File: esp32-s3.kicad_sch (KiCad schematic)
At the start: 21 parts, among them J3 Conn_01x07, Q1 2N7002, Q3 S8050, Q4 S8050, SW1 RESET, SW2 BOOT, U3 ESP32-S3-WROOM-1

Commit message: Pre-fab QA review fixes: switch input levels, power path, sensor spec, ESD
- R1-R8 switch series resistors 10k -> 1k: with only the ESP32 internal
  ~45k pull-up, 10k divided a closed switch to 0.6V vs the S3's 0.825V
  VIL limit — marginal. 1k gives ~0.1-0.23V worst case.
- U11 ACS723 -> ACS725LLCTR-05AB-T (C3684552): ACS723 needs 4.5-5.5V but
  ran at 3.3V (out of spec). ACS725 is 3.3V-native, same SOIC-8, rated
  to +150C. Firmware: sensitivity 264mV/A, formula (x-1.65)/0.264.
- D2 BAT54C (200mA) removed; replaced with D10/D11 SS34 (3A) diode-OR.
  The old diode carried the full ESP32 load permanently; WiFi TX bursts
  reach 350-500mA.
- U16 PRTR5V0U2X added on USB D+/D- (ESD protection at J2).
- D1 SS34 -> SS54 (5A, same SMA footprint) for multi-motor headroom.
- C10 bumped to 25V-rated 100uF 1210 (C2840614), same footprint.
- Filled all missing LCSC fields for JLCPCB assembly BOM.
- Docs: J4 pinout corrected to as-built; firmware bring-up checklist and
  RTS/DTR terminal gotcha added; CLAUDE.md placement guide for D10/D11/U16.

PCB placement of D10/D11/U16 + F8 sync still pending.

Co-Authored-By: Claude Fable 5 <noreply@anthropic.com>
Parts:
- C17: LCSC (none) -> C15849
- Q1: LCSC (none) -> C8545
- Q3, Q4: LCSC (none) -> C2146
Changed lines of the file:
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@@
+			)
+		)
+		(property "LCSC" "C8545"
+			(at 207.01 35.56 0)
+			(hide yes)
+			(show_name no)
+			(do_not_autoplace no)
+			(effects
+				(font
+					(size 1.27 1.27)
+				)
 			)
 		)
@@
 			)
 		)
+		(property "LCSC" "C15849"
+			(at 264.16 38.1 0)
+			(hide yes)
+			(show_name no)
+			(do_not_autoplace no)
+			(effects
+				(font
+					(size 1.27 1.27)
+				)
+			)
+		)
 		(pin "1"
 		)
@@
 			)
 		)
+		(property "LCSC" "C2146"
+			(at 262.89 77.47 0)
+			(hide yes)
+			(show_name no)
+			(do_not_autoplace no)
+			(effects
+				(font
+					(size 1.27 1.27)
+				)
+			)
+		)
 		(pin "1"
 		)
@@
 			(at 252.73 38.1 0)
 			(hide yes)
+			(show_name no)
+			(do_not_autoplace no)
+			(effects
+				(font
+					(size 1.27 1.27)
+				)
+			)
+		)
+		(property "LCSC" "C2146"
+			(at 252.73 38.1 0)
+			(hide yes)

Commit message: Rev 1.3 PCB sync + second QA pass: BOM fixes, TVS decoupling, ERC cleanup
PCB (done in KiCad, verified here):
- F8 sync applied: D2 removed; D10/D11 (SS34 SMA) and U16 (PRTR5V0U2X SOT-143)
  placed and routed; R1-R8 -> 1k, D1 -> SS54, C10 -> 25V, U11 -> ACS725 updated
  in place. Footprint-level diff confirms exactly the intended delta, nothing
  else moved. DRC 0 errors / 0 unconnected pads.

Schematic fixes from the second QA pass:
- R1-R8 had NO LCSC part number (value change had landed, part number never
  did) - they would have come back unpopulated, silently killing the switch
  inputs. Set to C14676, matching R14's existing 1K 0603 so it consolidates to
  one BOM line. NOTE: todo.md originally specified C21190 - see the discrepancy
  note there and confirm before ordering.
- TP1-TP7 set in_bom no / in_pos_files no (were 7 junk lines in the JLCPCB BOM).
- Removed 4 orphan dangling wire stubs in switch_inputs.kicad_sch.
- Converted the orphan STBY hierarchical label in motor_drivers.kicad_sch to a
  global label rather than deleting it: its wire actually carried U9 pin 19, so
  deleting dropped U9.19 off the STBY net. Converting keeps the connection and
  clears the ERC hier_label_mismatch.
- Added C40-C43 (100nF 0402, C1525) for U12-U15 VCC decoupling. The switch-input
  TVS devices currently have their nearest +3.3V_ISO bypass 18-23mm away; a
  PRTR5V0U2X shunts ESD into VCC and needs somewhere local to dump it. Still
  need PCB placement - put each within ~2mm of its device's pin 4.

Every schematic edit was validated by diffing the exported netlist before and
after; connectivity is unchanged apart from the four intended new caps.
ERC errors: 10 -> 5 (remaining are 4x missing PWR_FLAG and one J2-GND/U1-(-Vout)
both-power-output pair that is correct by design).

Added barn-blinds-controller.kicad_dru: isolation-barrier audit rule. The board
has no dedicated ISO/MOTOR gap - minimum copper spacing between domains is
0.20mm, the global default. Rev 1.2 measured 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
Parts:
- TP4, TP5: now left out of the parts list
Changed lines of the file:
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@@
 		(body_style 1)
 		(exclude_from_sim no)
-		(in_bom yes)
-		(on_board yes)
-		(in_pos_files yes)
+		(in_bom no)
+		(on_board yes)
+		(in_pos_files no)
 		(dnp no)
 		(fields_autoplaced yes)
@@
 		(body_style 1)
 		(exclude_from_sim no)
-		(in_bom yes)
-		(on_board yes)
-		(in_pos_files yes)
-		(dnp no)
-		(fields_autoplaced yes)
+		(in_bom no)
+		(on_board yes)
+		(in_pos_files no)
+		(dnp no)
+		(fields_autoplaced yes)

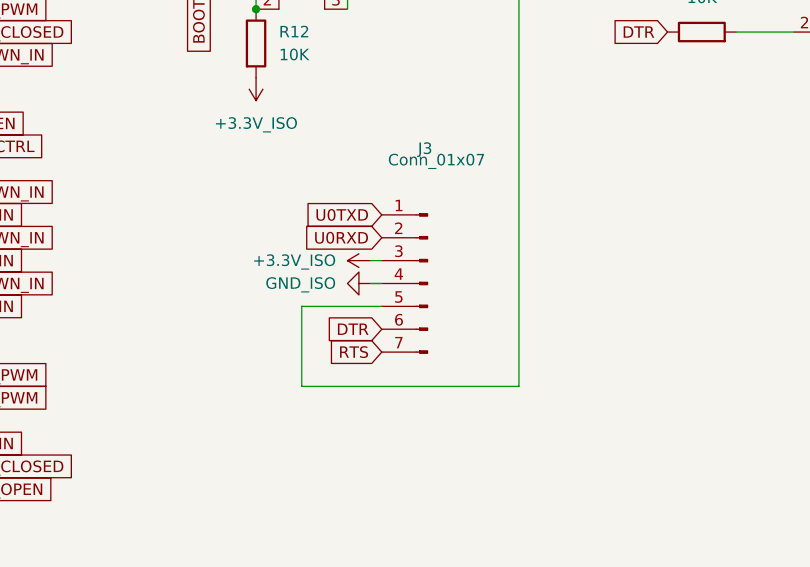
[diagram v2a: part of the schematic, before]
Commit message: Stock-driven part swaps (C10, U12-U16) + J3 DNP after BOM audit
C10 (isolated 5V_ISO bulk cap): 100uF 25V (C2840614) was out of stock at
JLCPCB. Swapped to 100uF 16V (C7432790, HGC1210R5107M160NSVK) - same 1210
footprint, no PCB rework. 16V chosen over 10V/6.3V alternatives to keep
DC-bias derating low on the ~5V rail (unregulated B1205S-3WR2L output).

U12-U16 (PRTR5V0U2X ESD protection): C12333 was out of stock. Swapped to
C5158049 (UMW/Youtai) - same SOT-143 footprint, no PCB rework. Checked
four other "PRTR5V0U2X"-labeled LCSC listings before picking this one -
they were mismatched (unidirectional, or 14-25V standoff instead of ~5V)
despite sharing the part name; C5158049 actually matches the real
bidirectional/0.35pF/5V-7.2V spec.

Both changes verified via netlist diff (only Value/LCSC fields changed,
zero connectivity impact) and ERC (still 5 known-benign errors).

Auditing the regenerated JLCPCB assembly-order BOM turned up a separate,
pre-existing bug: J3's LCSC (C492404) is a 5-pin header (PZ254V-11-05P),
mismatched against its 7-pin footprint - a leftover from before J3 grew
from 5->7 pins for the RTS/DTR rework, where the LCSC field (and a stale
"01x05" Description) never got updated. JLCPCB's assembly matcher didn't
flag the mismatch, it silently auto-substituted a different 5-pin part.
A real 7-pin replacement isn't in stock either, and J3 is only a backup
UART flashing path (native USB on GPIO19/20 is primary) - not worth
chasing for this run, so J3 is now marked DNP. Fixed the stale "01x05"
Description text to "01x07" so the record is correct if it's ever
un-DNP'd (LCSC still needs a real 7-pin part first if that happens).

PCB: C10/U12-U16 changes synced via F8. J3's new DNP flag still needs an
F8 sync (done after the schematic edit, not yet reflected on the board).

Updated CLAUDE.md PICK UP HERE and vsp-wsc4-todo.md with full detail.
VSP-WSC-4_1.3 production files predate all three changes - needs a
Fabrication Toolkit re-run before ordering.

Co-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
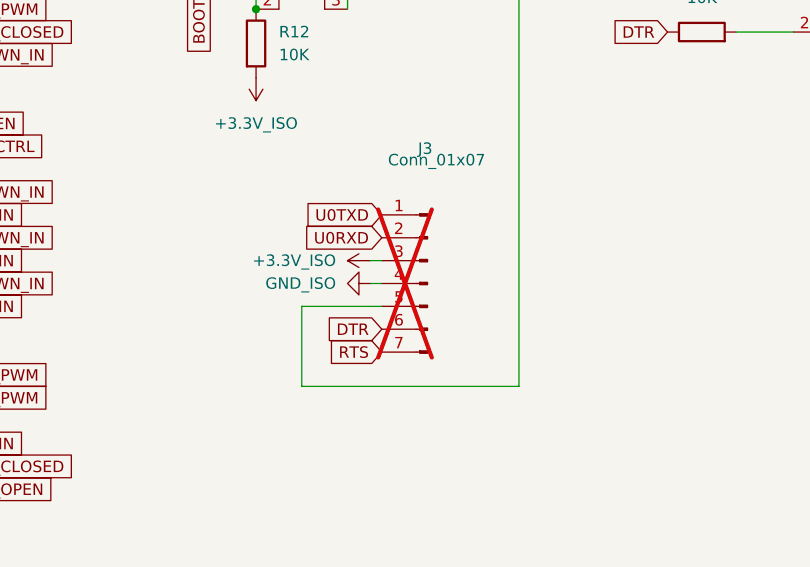
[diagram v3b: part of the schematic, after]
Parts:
- J3: now not fitted
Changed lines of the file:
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@@
 		(on_board yes)
 		(in_pos_files yes)
-		(dnp no)
+		(dnp yes)
 		(property "Reference" "J3"
 			(at 216.916 90.424 0)
@@
 			)
 		)
-		(property "Description" "Generic connector, single row, 01x05, script generated"
+		(property "Description" "Generic connector, single row, 01x07, script generated"
 			(at 217.17 105.41 0)
 			(hide yes)
